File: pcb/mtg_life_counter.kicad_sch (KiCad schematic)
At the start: 41 parts, among them J1 GCT USB-4135-GF-A, J2 ICSP, J3 TP_UART, SW1 MODE SW, SW2 MODE SW, U1 ATmega328P-AU, Y1 16MHz

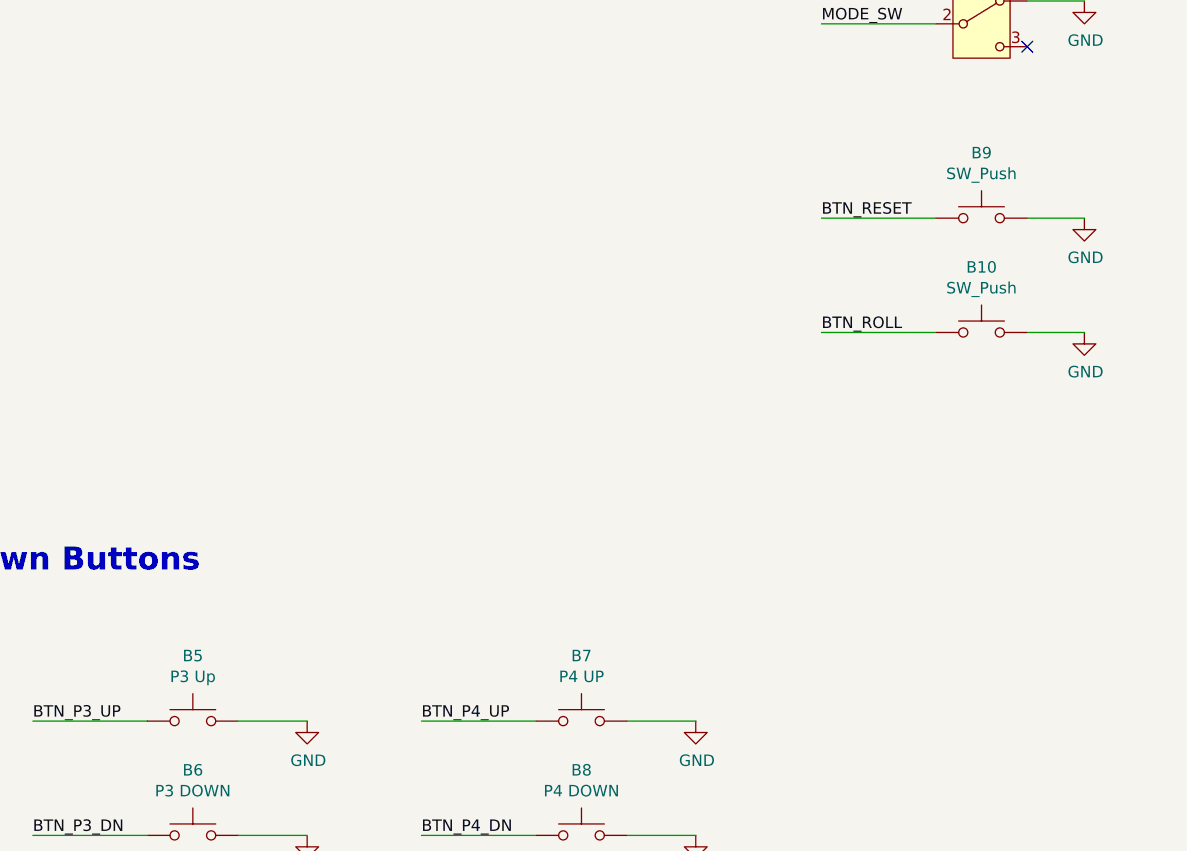
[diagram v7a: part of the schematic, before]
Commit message: button text alignment
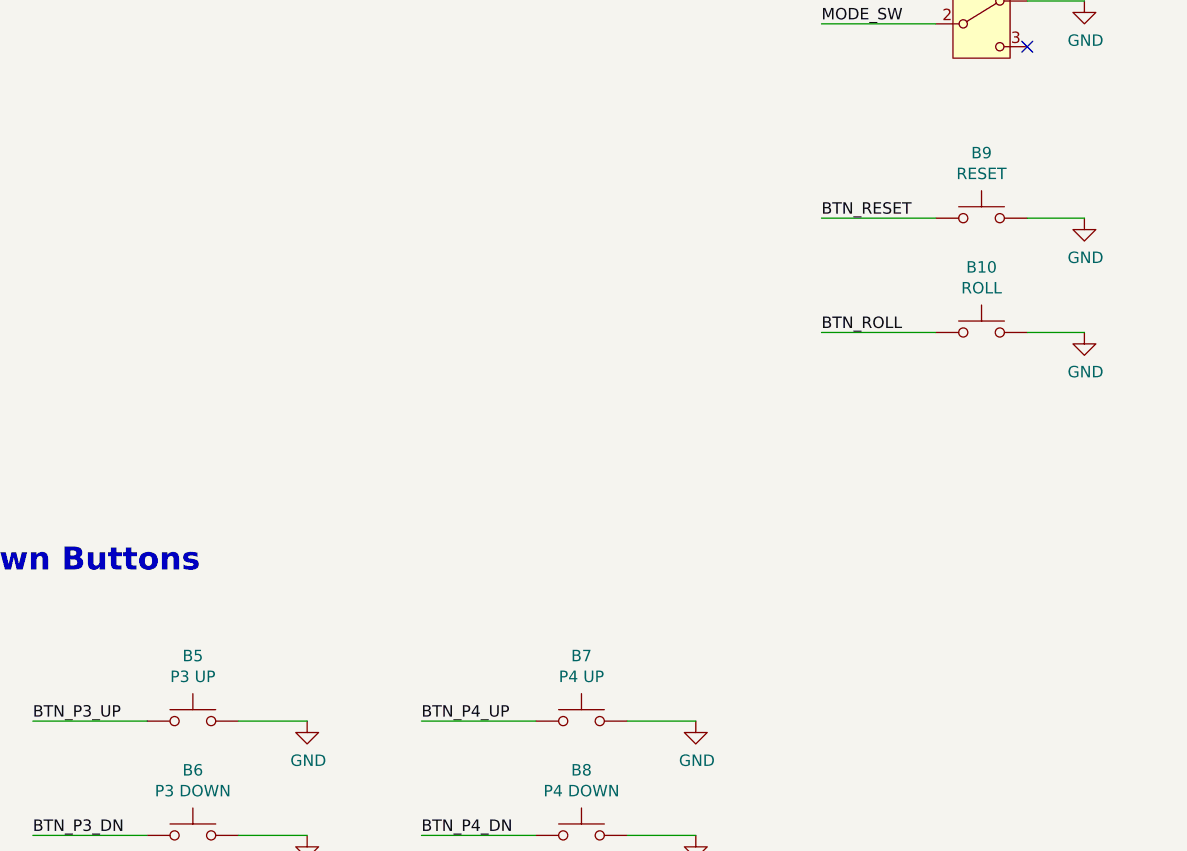
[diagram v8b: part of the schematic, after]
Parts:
- B10: value SW_Push -> ROLL
- B5: value P3 Up -> P3 UP
- B9: value SW_Push -> RESET
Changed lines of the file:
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@@
 			)
 		)
-		(property "Value" "SW_Push"
+		(property "Value" "RESET"
 			(at 224.79 160.1724 0)
 			(effects
@@
 			)
 		)
-		(property "Value" "SW_Push"
+		(property "Value" "ROLL"
 			(at 224.79 172.8724 0)
 			(effects
@@
 			)
 		)
-		(property "Value" "P3 Up"
+		(property "Value" "P3 UP"
 			(at 137.16 216.0524 0)
 			(effects
